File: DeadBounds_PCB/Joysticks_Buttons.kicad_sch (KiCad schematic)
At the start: 0 parts

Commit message: Added LED Drivers and Joysticks
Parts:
- added Joystick1(Move), Joystick2(Look): Conn_01x05_Socket, symbol Connector:Conn_01x05_Socket
- added Trigger: SW_Push, symbol Switch:SW_Push
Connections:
- new net +5V: Joystick1(Move).4 (Pin_4), Joystick2(Look).4 (Pin_4)
- new net GND: Joystick1(Move).5 (Pin_5), Joystick2(Look).5 (Pin_5), Trigger.2
- new net SW1: Joystick1(Move).1 (Pin_1)
- new net SW2: Joystick2(Look).1 (Pin_1)
- new net SWShoot: Trigger.1
- new net VRX1: Joystick1(Move).3 (Pin_3)
- new net VRX2: Joystick2(Look).3 (Pin_3)
- new net VRY1: Joystick1(Move).2 (Pin_2)
- new net VRY2: Joystick2(Look).2 (Pin_2)

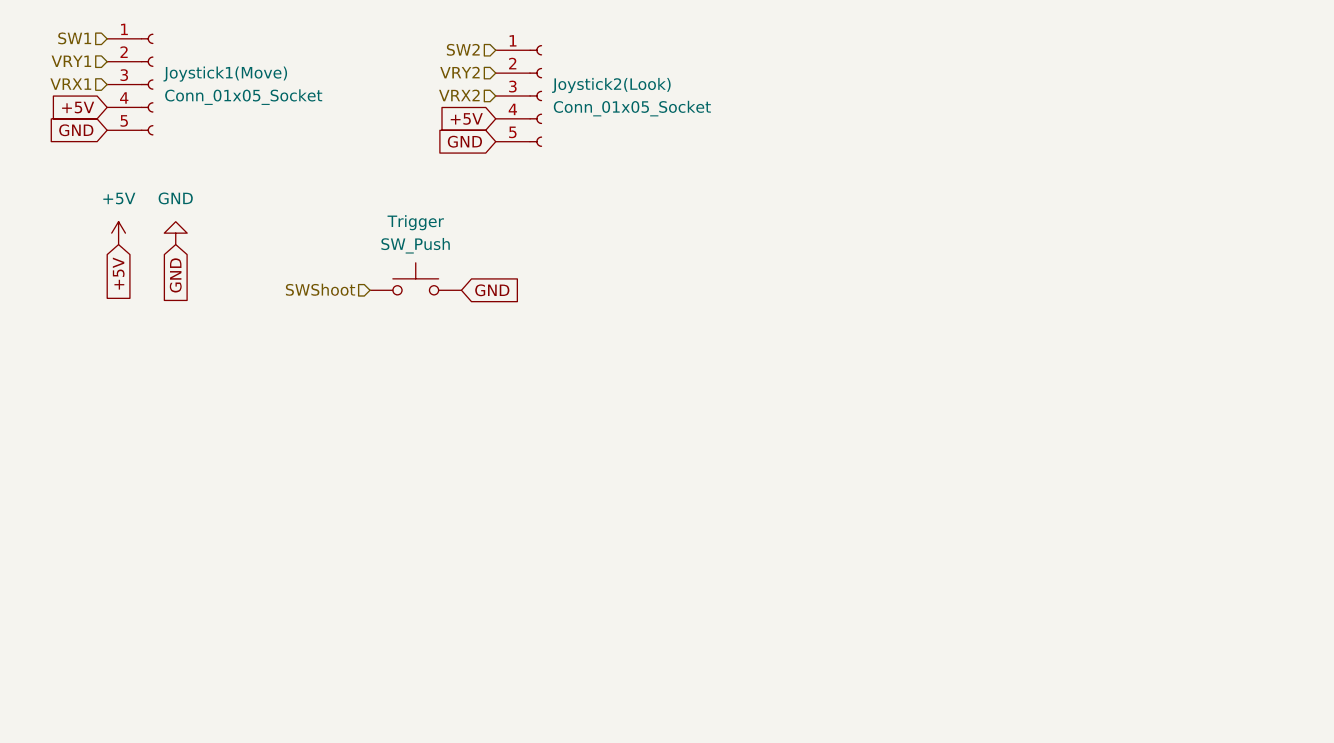
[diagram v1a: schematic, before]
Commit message: Finished schematics, assigned/made footprints except for resistors
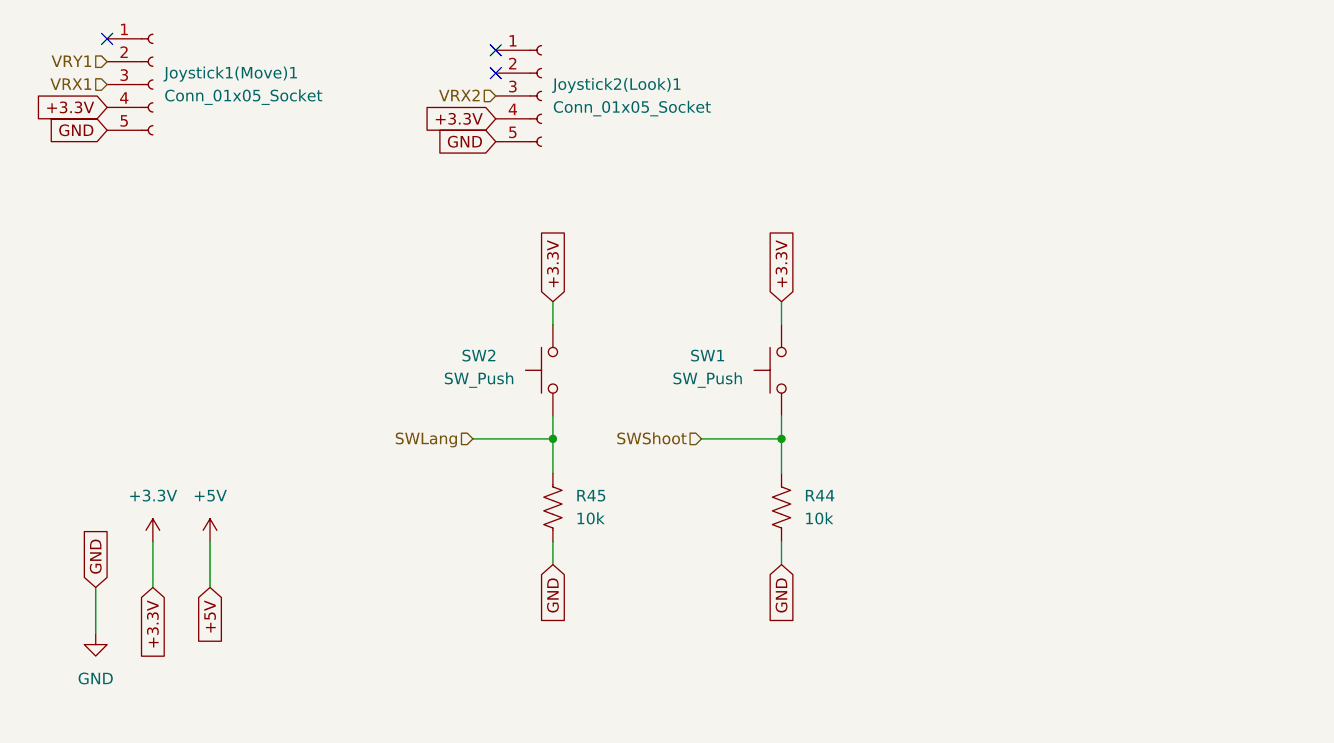
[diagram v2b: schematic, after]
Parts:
- added R44, R45: 10k, symbol Device:R_US
- added SW2: SW_Push, Button_Switch_THT:SW_TH_Tactile_Omron_B3F-102x, symbol Switch:SW_Push
- Joystick1(Move)1: renamed from Joystick1(Move); footprint (none) -> Connector_PinSocket_2.54mm:PinSocket_1x05_P2.54mm_Horizontal
- Joystick2(Look)1: renamed from Joystick2(Look); footprint (none) -> Connector_PinSocket_2.54mm:PinSocket_1x05_P2.54mm_Horizontal
- SW1: renamed from Trigger; footprint (none) -> Button_Switch_THT:SW_TH_Tactile_Omron_B3F-106x
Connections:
- net +5V: no longer Joystick1(Move)1.4 (Pin_4), Joystick2(Look)1.4 (Pin_4)
- net GND: now also R44.2, R45.2; no longer SW1.2
- net SWShoot: now also R44.1
- net SW1: no longer names the net of Joystick1(Move)1.1 (Pin_1)
- net SW2: no longer names the net of Joystick2(Look)1.1 (Pin_1)
- net VRY2: no longer names the net of Joystick2(Look)1.2 (Pin_2)
- new net +3.3V: Joystick1(Move)1.4 (Pin_4), Joystick2(Look)1.4 (Pin_4), SW1.2, SW2.2
- new net SWLang: R45.1, SW2.1
- no-connect marks 0 -> 3
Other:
- moved on the sheet: SW1

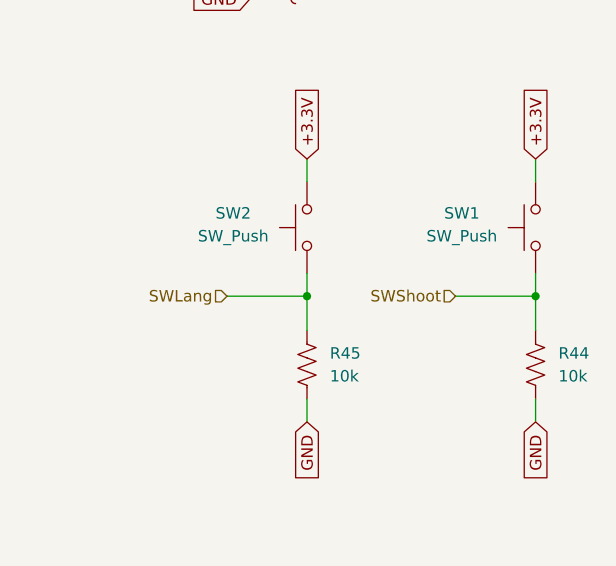
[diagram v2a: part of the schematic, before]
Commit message: MCU wiring and LED resistance edits
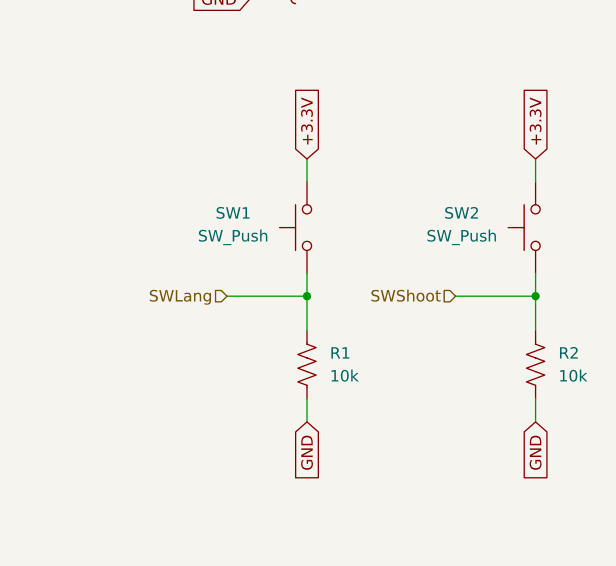
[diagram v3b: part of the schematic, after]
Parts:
- R1: renamed from R45; footprint (none) -> Resistor_THT:R_Axial_DIN0207_L6.3mm_D2.5mm_P7.62mm_Horizontal
- R2: renamed from R44; footprint (none) -> Resistor_THT:R_Axial_DIN0207_L6.3mm_D2.5mm_P7.62mm_Horizontal
- renumbered SW2 to SW1, SW1 to SW2
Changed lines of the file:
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@@
 		(in_pos_files yes)
 		(dnp no)
-		(property "Reference" "SW1"
+		(property "Reference" "SW2"
 			(at 99.7585 55.5625 90)
 			(show_name no)
@@
 			(project "DeadBounds_PCB"
 				(path "/c652495f-dd42-4f45-9891-1e05b67942c0/647be0ff-a9ec-4a97-94e4-73e3782c2387"
-					(reference "SW1")
+					(reference "SW2")
 					(unit 1)
 				)
@@
 		(in_pos_files yes)
 		(dnp no)
-		(property "Reference" "SW2"
+		(property "Reference" "SW1"
 			(at 74.3585 55.5625 90)
 			(show_name no)
@@
 			(project "DeadBounds_PCB"
 				(path "/c652495f-dd42-4f45-9891-1e05b67942c0/647be0ff-a9ec-4a97-94e4-73e3782c2387"
-					(reference "SW2")
+					(reference "SW1")
 					(unit 1)
 				)
@@
 		(dnp no)
 		(fields_autoplaced yes)
-		(property "Reference" "R44"
+		(property "Reference" "R2"
 			(at 110.49 71.1199 0)
 			(show_name no)
@@
 			)
 		)
-		(property "Footprint" ""
+		(property "Footprint" "Resistor_THT:R_Axial_DIN0207_L6.3mm_D2.5mm_P7.62mm_Horizontal"
 			(at 108.966 72.644 90)
 			(hide yes)
@@
 			(project "DeadBounds_PCB"
 				(path "/c652495f-dd42-4f45-9891-1e05b67942c0/647be0ff-a9ec-4a97-94e4-73e3782c2387"
-					(reference "R44")
+					(reference "R2")
 					(unit 1)
 				)
@@
 		(dnp no)
 		(fields_autoplaced yes)
-		(property "Reference" "R45"
+		(property "Reference" "R1"
 			(at 85.09 71.1199 0)
 			(show_name no)
@@
 			)
 		)
-		(property "Footprint" ""
+		(property "Footprint" "Resistor_THT:R_Axial_DIN0207_L6.3mm_D2.5mm_P7.62mm_Horizontal"
 			(at 83.566 72.644 90)
 			(hide yes)
@@
 			(project "DeadBounds_PCB"
 				(path "/c652495f-dd42-4f45-9891-1e05b67942c0/647be0ff-a9ec-4a97-94e4-73e3782c2387"
-					(reference "R45")
-					(unit 1)
-				)
+					(reference "R1")
+					(unit 1)
+				)

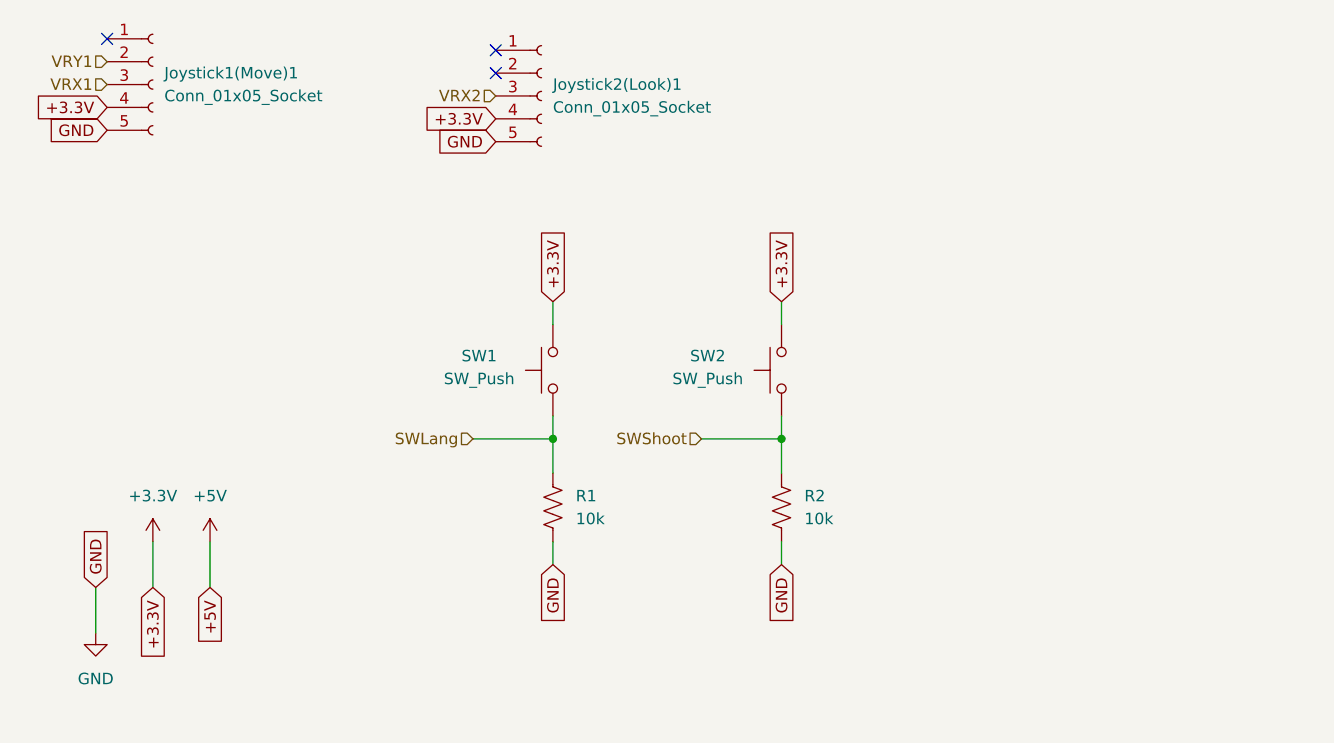
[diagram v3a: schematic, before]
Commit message: Added amplifier circuit and additional jumpers to PCB
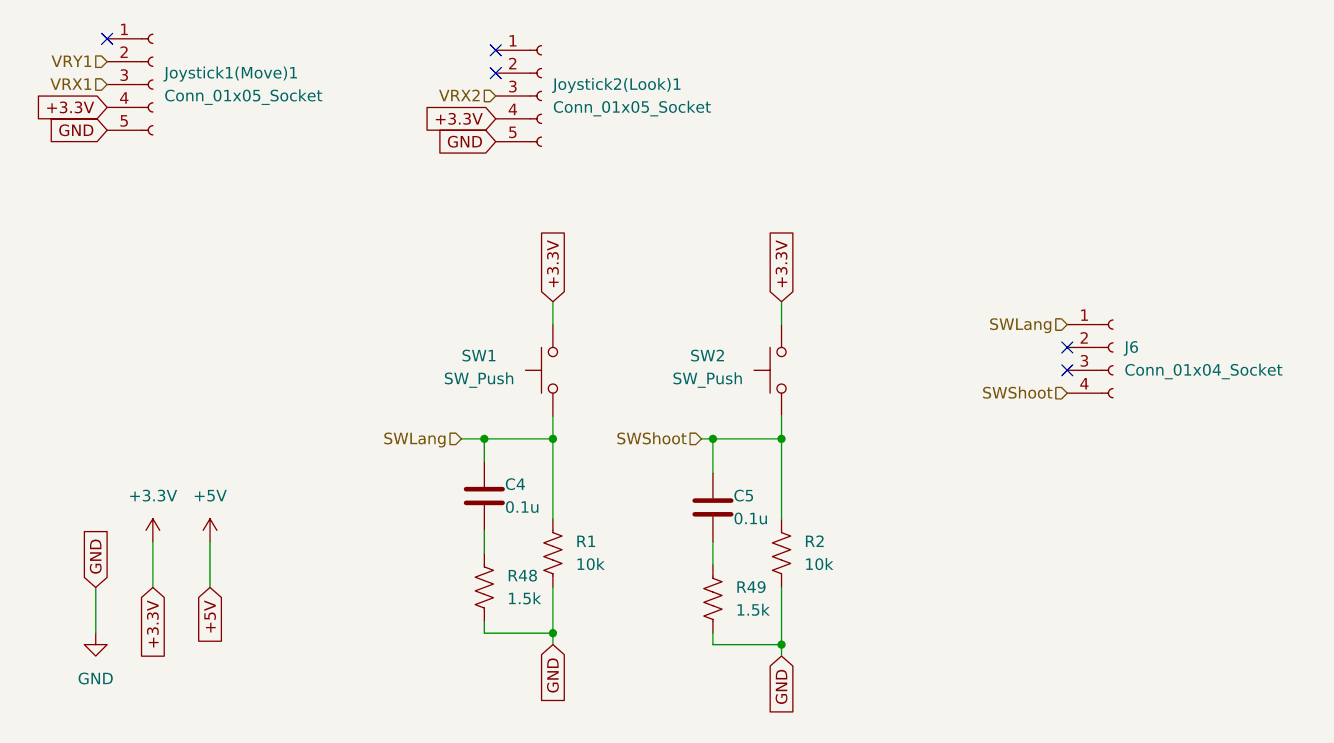
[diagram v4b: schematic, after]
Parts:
- added C4, C5: 0.1u, ECE319K:C_Axial_200mil, symbol DeadBounds_Symbols:C
- added J6: Conn_01x04_Socket, Connector_PinSocket_2.54mm:PinSocket_1x04_P2.54mm_Horizontal, symbol Connector:Conn_01x04_Socket
- added R48, R49: 1.5k, Resistor_THT:R_Axial_DIN0207_L6.3mm_D2.5mm_P7.62mm_Horizontal, symbol Device:R_US
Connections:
- net GND: now also R48.2, R49.2
- net SWLang: now also C4.1, J6.1 (Pin_1)
- net SWShoot: now also C5.1, J6.4 (Pin_4)
- new net: C4.2, R48.1
- new net: C5.2, R49.1
- no-connect marks 3 -> 5
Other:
- moved on the sheet: R1, R2
